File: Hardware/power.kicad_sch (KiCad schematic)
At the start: 0 parts

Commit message: Added 3.3V power connections and a USB-C connector for +5V
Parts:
- added C1: 100uF, C3225X5R0J107M250AB:CAP_C3225X5R0J107M250AB, symbol C3225X5R0J107M250AB:C3225X5R0J107M250AB
- added C2: 47uF, C3225X5R0J476M250AA:CAP_C3225X5R0J476M250AA, symbol C3225X5R0J476M250AA:C3225X5R0J476M250AA
- added C3: 100nF, C0402C104J8RACTU:CAPC10555_55N_KEM-L, symbol 2025-06-22_21-59-05:C0402C104J8RACTU
- added L1: MSS1038-152NLC, Inductor_SMD:L_Coilcraft_MSS1038-XXX, symbol MSS1038-152NLC:MSS1038-152NLC
- added P1: USB_C_Plug_USB2.0, Connector_USB:USB_C_Receptacle_GCT_USB4105-xx-A_16P_TopMnt_Horizontal, symbol Connector:USB_C_Plug_USB2.0
- added R5: 10k, Resistor_SMD:R_0402_1005Metric, symbol Device:R
- added R6: 10, Resistor_SMD:R_0402_1005Metric, symbol Device:R
- added U4: ADP2164ACPZ-3.3-R7, ADP2164ACPZ_3_3_R7:QFN65P400X400X80-17N, symbol ADP2164ACPZ-3.3-R7:ADP2164ACPZ-3.3-R7
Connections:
- new net: L1.1, U4.10 (SW__1), U4.11 (SW__2), U4.9 (SW)
- new net: C3.1, R5.1, R6.2, U4.1 (SYNC), U4.14 (VIN), U4.15 (EN), U4.2 (RT), U4.3 (TRK)
- new net: R5.2, U4.16 (PGOOD)
- new net +3.3V: C1.1, L1.2, U4.4 (FB)
- new net +5V: C2.1, P1.A4 (VBUS), P1.A9 (VBUS), P1.B4 (VBUS), P1.B9 (VBUS), R6.1, U4.12 (PVIN), U4.13 (PVIN__1)
- new net GND: C1.2, C2.2, C3.2, P1.A1 (GND), P1.A12 (GND), P1.B1 (GND), P1.B12 (GND), P1.S1 (SHIELD), U4.17 (EP), U4.5 (GND), U4.6 (PGND), U4.7 (PGND__1), U4.8 (PGND__2)
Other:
- company: (none) -> Thomas Montano
- title: (none) -> 3.3V Power Block

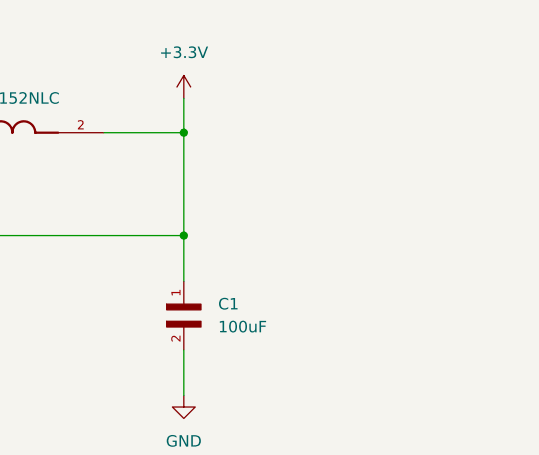
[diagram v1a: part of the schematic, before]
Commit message: added filtering caps, bulk decoupling caps, and power LED
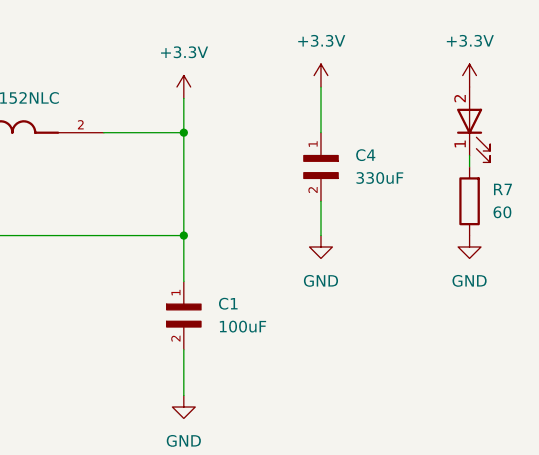
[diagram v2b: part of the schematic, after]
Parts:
- added C4: 330uF, TRME337K010R0035:CAPPM7343X310N, symbol TRME337K010R0035:TRME337K010R0035
- added LED1: CMD17-21VGD/TR8, CMD17_21VGD_TR8:LED0805N_CML-M, symbol 2025-06-23_02-31-26:CMD17-21VGD_TR8
- added R7: 60, Resistor_SMD:R_0402_1005Metric, symbol Device:R
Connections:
- net +3.3V: now also C4.1, LED1.2
- net GND: now also C4.2, R7.1
- new net: LED1.1, R7.2

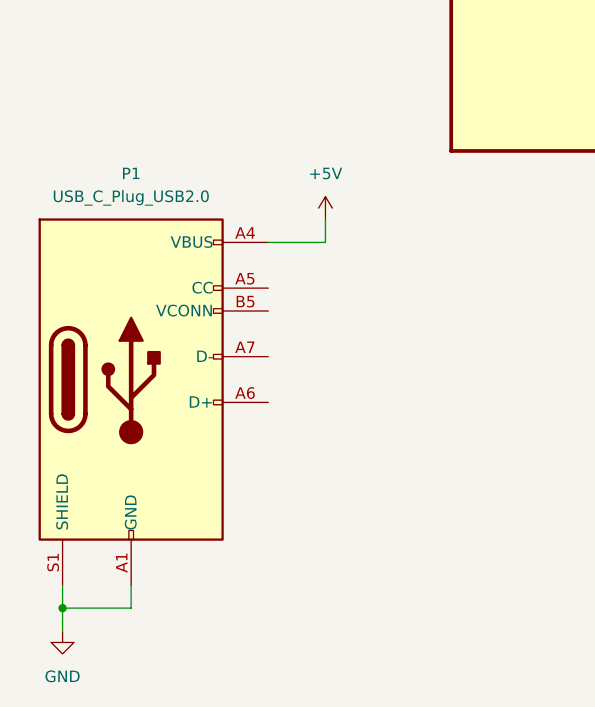
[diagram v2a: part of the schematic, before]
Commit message: added SMA connectors and external connections sheet
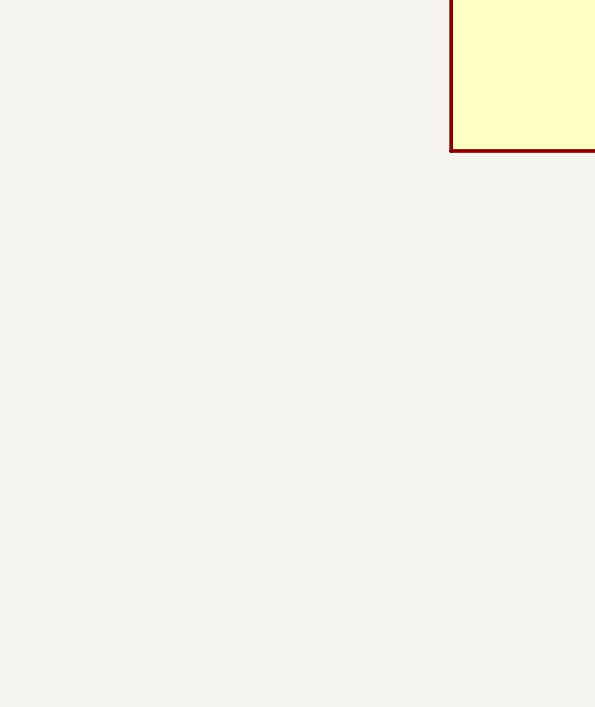
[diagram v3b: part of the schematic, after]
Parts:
- removed P1: USB_C_Plug_USB2.0, Connector_USB:USB_C_Receptacle_GCT_USB4105-xx-A_16P_TopMnt_Horizontal, symbol Connector:USB_C_Plug_USB2.0

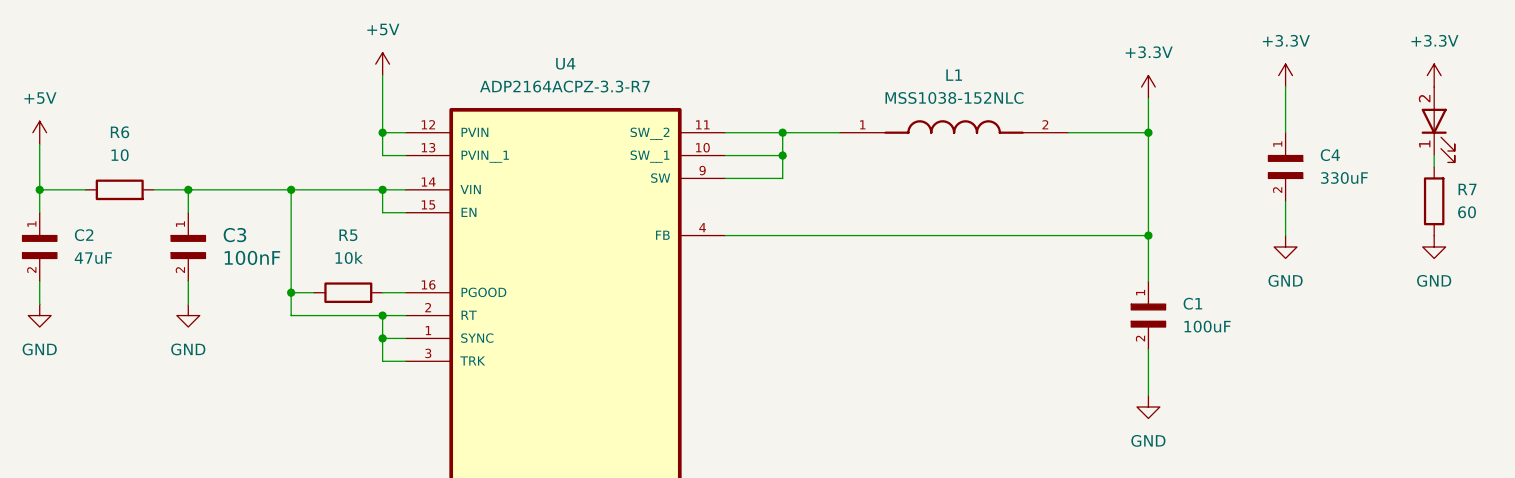
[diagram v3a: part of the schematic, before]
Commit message: Finished Ethernet connection between MAC and PHY
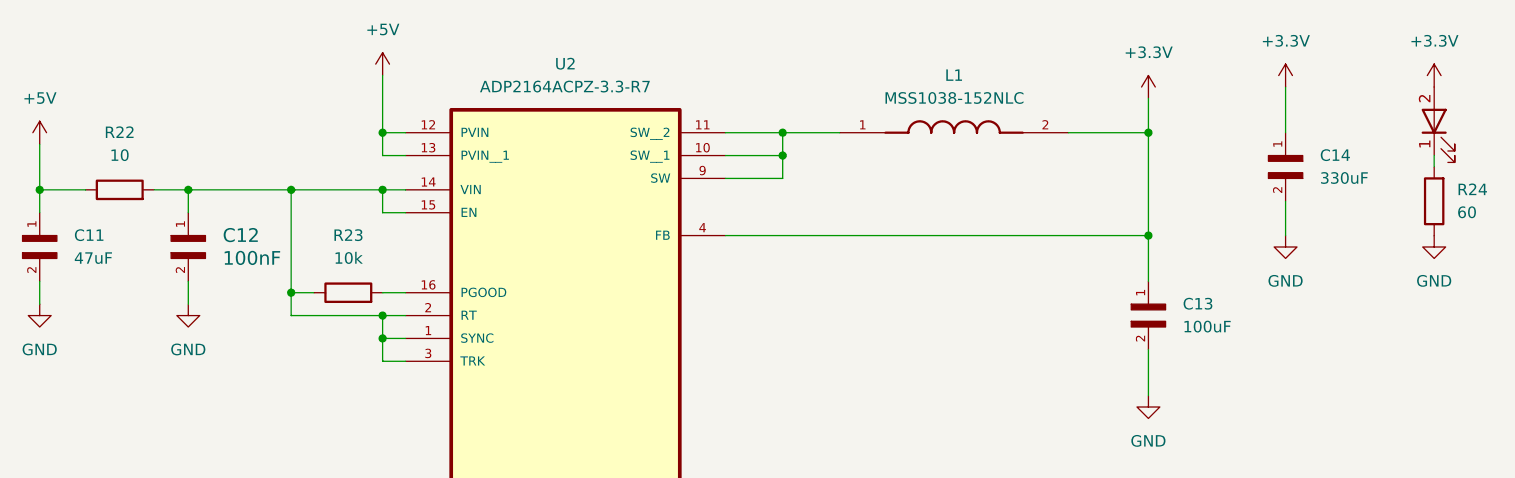
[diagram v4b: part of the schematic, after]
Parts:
- renumbered C2 to C11, C3 to C12, C1 to C13, C4 to C14, R6 to R22, R5 to R23, R7 to R24, U4 to U2
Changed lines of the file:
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@@
 		(dnp no)
 		(fields_autoplaced yes)
-		(property "Reference" "C4"
+		(property "Reference" "C14"
 			(at 170.18 67.3099 90)
 			(effects
@@
 			(project ""
 				(path "/ca6389fe-9846-40e3-87a4-456cfcfc0777/bd0f5978-e4b1-41e2-96b4-94a3773ac12f"
-					(reference "C4")
+					(reference "C14")
 					(unit 1)
 				)
@@
 		(dnp no)
 		(fields_autoplaced yes)
-		(property "Reference" "R6"
+		(property "Reference" "R22"
 			(at 36.83 64.77 90)
 			(effects
@@
 			(project "Radio Project"
 				(path "/ca6389fe-9846-40e3-87a4-456cfcfc0777/bd0f5978-e4b1-41e2-96b4-94a3773ac12f"
-					(reference "R6")
+					(reference "R22")
 					(unit 1)
 				)
@@
 		(dnp no)
 		(fields_autoplaced yes)
-		(property "Reference" "#PWR014"
+		(property "Reference" "#PWR016"
 			(at 151.13 64.77 0)
 			(effects
@@
 			(project "Radio Project"
 				(path "/ca6389fe-9846-40e3-87a4-456cfcfc0777/bd0f5978-e4b1-41e2-96b4-94a3773ac12f"
-					(reference "#PWR014")
+					(reference "#PWR016")
 					(unit 1)
 				)
@@
 		(dnp no)
 		(fields_autoplaced yes)
-		(property "Reference" "#PWR018"
+		(property "Reference" "#PWR011"
 			(at 27.94 69.85 0)
 			(effects
@@
 			(project "Radio Project"
 				(path "/ca6389fe-9846-40e3-87a4-456cfcfc0777/bd0f5978-e4b1-41e2-96b4-94a3773ac12f"
-					(reference "#PWR018")
+					(reference "#PWR011")
 					(unit 1)
 				)
@@
 		(dnp no)
 		(fields_autoplaced yes)
-		(property "Reference" "R7"
+		(property "Reference" "R24"
 			(at 185.42 71.1199 0)
 			(effects
@@
 			(project "Radio Project"
 				(path "/ca6389fe-9846-40e3-87a4-456cfcfc0777/bd0f5978-e4b1-41e2-96b4-94a3773ac12f"
-					(reference "R7")
+					(reference "R24")
 					(unit 1)
 				)
@@
 		(dnp no)
 		(fields_autoplaced yes)
-		(property "Reference" "#PWR023"
+		(property "Reference" "#PWR018"
 			(at 166.37 63.5 0)
 			(effects
@@
 			(project "Radio Project"
 				(path "/ca6389fe-9846-40e3-87a4-456cfcfc0777/bd0f5978-e4b1-41e2-96b4-94a3773ac12f"
-					(reference "#PWR023")
+					(reference "#PWR018")
 					(unit 1)
 				)
@@
 		(dnp no)
 		(fields_autoplaced yes)
-		(property "Reference" "#PWR025"
+		(property "Reference" "#PWR020"
 			(at 182.88 63.5 0)
 			(effects
@@
 			(project "Radio Project"
 				(path "/ca6389fe-9846-40e3-87a4-456cfcfc0777/bd0f5978-e4b1-41e2-96b4-94a3773ac12f"
-					(reference "#PWR025")
+					(reference "#PWR020")
 					(unit 1)
 				)
@@
 		(dnp no)
 		(fields_autoplaced yes)
-		(property "Reference" "C1"
+		(property "Reference" "C13"
 			(at 154.94 83.8199 90)
 			(effects
@@
 			(project ""
 				(path "/ca6389fe-9846-40e3-87a4-456cfcfc0777/bd0f5978-e4b1-41e2-96b4-94a3773ac12f"
-					(reference "C1")
+					(reference "C13")
 					(unit 1)
 				)
@@
 		(dnp no)
 		(fields_autoplaced yes)
-		(property "Reference" "#PWR016"
+		(property "Reference" "#PWR017"
 			(at 151.13 100.33 0)
 			(effects
@@
 			(project "Radio Project"
 				(path "/ca6389fe-9846-40e3-87a4-456cfcfc0777/bd0f5978-e4b1-41e2-96b4-94a3773ac12f"
-					(reference "#PWR016")
+					(reference "#PWR017")
 					(unit 1)
 				)
@@
 		(dnp no)
 		(fields_autoplaced yes)
-		(property "Reference" "C3"
+		(property "Reference" "C12"
 			(at 48.26 76.1999 90)
 			(effects
@@
 			(project ""
 				(path "/ca6389fe-9846-40e3-87a4-456cfcfc0777/bd0f5978-e4b1-41e2-96b4-94a3773ac12f"
-					(reference "C3")
+					(reference "C12")
 					(unit 1)
 				)
@@
 		(dnp no)
 		(fields_autoplaced yes)
-		(property "Reference" "#PWR020"
+		(property "Reference" "#PWR013"
 			(at 44.45 90.17 0)
 			(effects
@@
 			(project "Radio Project"
 				(path "/ca6389fe-9846-40e3-87a4-456cfcfc0777/bd0f5978-e4b1-41e2-96b4-94a3773ac12f"
-					(reference "#PWR020")
+					(reference "#PWR013")
 					(unit 1)
 				)
@@
 		(dnp no)
 		(fields_autoplaced yes)
-		(property "Reference" "C2"
+		(property "Reference" "C11"
 			(at 31.75 76.1999 90)
 			(effects
@@
 			(project ""
 				(path "/ca6389fe-9846-40e3-87a4-456cfcfc0777/bd0f5978-e4b1-41e2-96b4-94a3773ac12f"
-					(reference "C2")
+					(reference "C11")
 					(unit 1)
 				)
@@
 		(dnp no)
 		(fields_autoplaced yes)
-		(property "Reference" "#PWR026"
+		(property "Reference" "#PWR021"
 			(at 182.88 82.55 0)
 			(effects
@@
 			(project "Radio Project"
 				(path "/ca6389fe-9846-40e3-87a4-456cfcfc0777/bd0f5978-e4b1-41e2-96b4-94a3773ac12f"
-					(reference "#PWR026")
+					(reference "#PWR021")
 					(unit 1)
 				)
@@
 		(dnp no)
 		(fields_autoplaced yes)
-		(property "Reference" "#PWR017"
+		(property "Reference" "#PWR014"
 			(at 66.04 62.23 0)
 			(effects
@@
 			(project ""
 				(path "/ca6389fe-9846-40e3-87a4-456cfcfc0777/bd0f5978-e4b1-41e2-96b4-94a3773ac12f"
-					(reference "#PWR017")
+					(reference "#PWR014")
 					(unit 1)
 				)
@@
 		(dnp no)
 		(fields_autoplaced yes)
-		(property "Reference" "#PWR019"
+		(property "Reference" "#PWR012"
 			(at 27.94 90.17 0)
 			(effects
@@
 			(project "Radio Project"
 				(path "/ca6389fe-9846-40e3-87a4-456cfcfc0777/bd0f5978-e4b1-41e2-96b4-94a3773ac12f"
-					(reference "#PWR019")
+					(reference "#PWR012")
 					(unit 1)
 				)
@@
 		(dnp no)
 		(fields_autoplaced yes)
-		(property "Reference" "U4"
+		(property "Reference" "U2"
 			(at 86.36 57.15 0)
 			(effects
@@
 			(project ""
 				(path "/ca6389fe-9846-40e3-87a4-456cfcfc0777/bd0f5978-e4b1-41e2-96b4-94a3773ac12f"
-					(reference "U4")
+					(reference "U2")
 					(unit 1)
 				)
@@
 		(dnp no)
 		(fields_autoplaced yes)
-		(property "Reference" "R5"
+		(property "Reference" "R23"
 			(at 62.23 76.2 90)
 			(effects
@@
 			(project "Radio Project"
 				(path "/ca6389fe-9846-40e3-87a4-456cfcfc0777/bd0f5978-e4b1-41e2-96b4-94a3773ac12f"
-					(reference "R5")
+					(reference "R23")
 					(unit 1)
 				)
@@
 		(dnp no)
 		(fields_autoplaced yes)
-		(property "Reference" "#PWR024"
+		(property "Reference" "#PWR019"
 			(at 166.37 82.55 0)
 			(effects
@@
 			(project "Radio Project"
 				(path "/ca6389fe-9846-40e3-87a4-456cfcfc0777/bd0f5978-e4b1-41e2-96b4-94a3773ac12f"
-					(reference "#PWR024")
-					(unit 1)
-				)
+					(reference "#PWR019")
+					(unit 1)
+				)
